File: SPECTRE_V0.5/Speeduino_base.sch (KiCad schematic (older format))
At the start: 185 parts, among them J1 Conn_01x04_Male, J2 Conn_02x04_Odd_Even, J3 Conn_01x06_Male, Q1 2N7002, Q10 BSP78, Q11 BSP78, Q12 BSP78, Q13 BSP78, Q14 BSP78, Q15 BSP78, Q16 BSP78, Q17 BSP78, Q18 BSP78, Q2 CJ2302, Q3 CJ2302, Q4 CJ2302, Q5 BSP78, Q6 BSP78, Q7 CJ2302, Q8 CJ2302, Q9 CJ2302, U1 MAX9926UAEE+, U2 molex_48pin, U3 LM78M05_TO220, U4 MAX3232

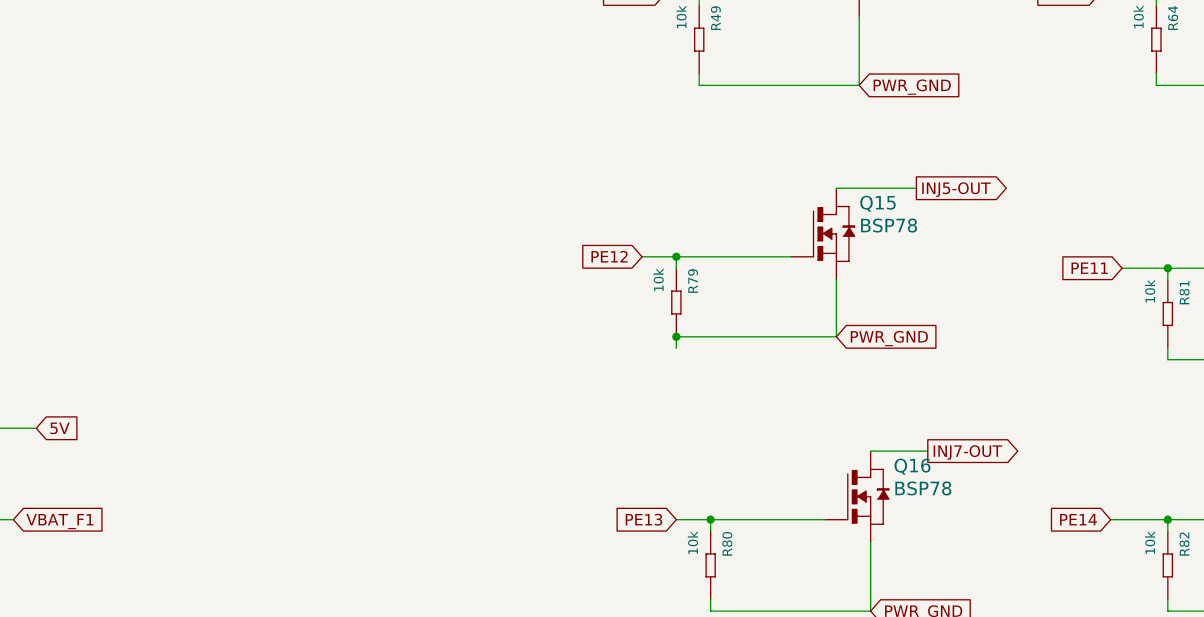
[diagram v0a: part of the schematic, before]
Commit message: update silkscreen
Updated silkscreen V0.4. Start switchable flyback diode in V0.5 for PWM control of injectors
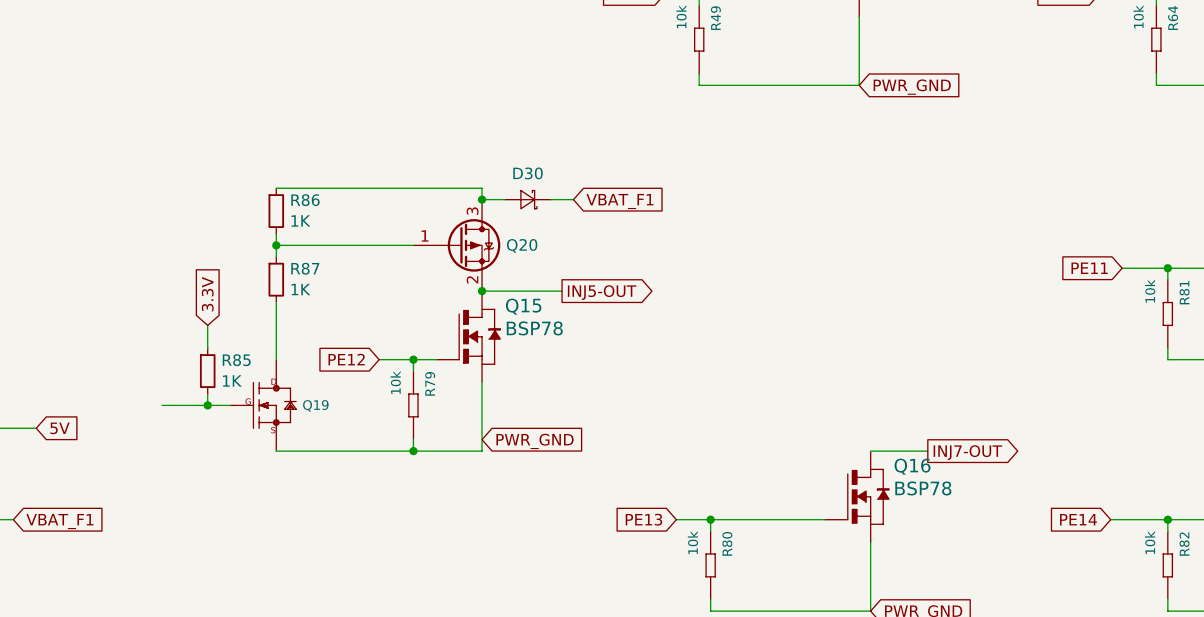
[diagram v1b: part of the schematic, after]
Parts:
- added D30: SS310, Diode_SMD:D_SMA, symbol Device:D_Schottky_Small
- added Q19: SMD-MOSFET-N-CH-30V-5.8A-AO3400(SOT-23), Package_TO_SOT_SMD:SOT-23_Handsoldering, symbol speeduino_lib:SMD-MOSFET-N-CH-30V-5.8A-AO3400(SOT-23)
- added Q20: AO3401A, Package_TO_SOT_SMD:SOT-23, symbol Transistor_FET:AO3401A
- added R85, R86, R87: 1K, Resistor_SMD:R_0603_1608Metric_Pad1.05x0.95mm_HandSolder, symbol Device:R_Small
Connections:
- wire segments 502 -> 515
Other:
- moved on the sheet: Q15, R79
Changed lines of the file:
@@
 	14100 11500 14100 11200
 Wire Wire Line
-	13950 10300 13950 10050
-Wire Wire Line
 	15400 10350 15400 10400
 Wire Wire Line
@@
 	16100 11500 16100 11200
 Wire Wire Line
-	13250 10000 13250 9950
+	12100 10450 12100 10400
 Wire Wire Line
 	15400 10050 15400 10000
@@
 L Speeduino_base-eagle-import:NMOSSOT223 Q15
 U 1 1 6231F413
-P 13950 9850
-F 0 "Q15" H 14050 9950 59  0000 L BNN
-F 1 "BSP78" H 14050 9850 59  0000 L BNN
-F 2 "Speeduino_base:SOT223" H 13950 9850 50  0001 C CNN
-F 3 "" H 13950 9850 50  0001 C CNN
-	1    13950 9850
+P 12400 10300
+F 0 "Q15" H 12500 10400 59  0000 L BNN
+F 1 "BSP78" H 12500 10300 59  0000 L BNN
+F 2 "Speeduino_base:SOT223" H 12400 10300 50  0001 C CNN
+F 3 "" H 12400 10300 50  0001 C CNN
+	1    12400 10300
 	1    0    0    -1
 $EndComp
@@
 L Speeduino_base-eagle-import:SMD-RES-470R-5%-1_10W(0603) R79
 U 1 1 6231F42B
-P 13250 10150
-F 0 "R79" H 13100 10200 42  0000 L BNN
-F 1 "10k" H 13100 10050 42  0000 L BNN
-F 2 "Speeduino_base:R0603" H 13250 10150 50  0001 C CNN
-F 3 "" H 13250 10150 50  0001 C CNN
-	1    13250 10150
+P 12100 10600
+F 0 "R79" H 11950 10650 42  0000 L BNN
+F 1 "10k" H 11950 10500 42  0000 L BNN
+F 2 "Speeduino_base:R0603" H 12100 10600 50  0001 C CNN
+F 3 "" H 12100 10600 50  0001 C CNN
+	1    12100 10600
 	0    1    1    0
 $EndComp
@@
 	0    1    1    0
 $EndComp
-Text GLabel 13100 9950 0    50   Input ~ 0
+Text GLabel 11950 10400 0    50   Input ~ 0
 PE12
 Text GLabel 13250 11100 0    50   Input ~ 0
@@
 PE14
 Wire Wire Line
-	13100 9950 13250 9950
-Connection ~ 13250 9950
-Wire Wire Line
-	13250 9950 13750 9950
+	11950 10400 12100 10400
 Wire Wire Line
 	13250 11100 13400 11100
@@
 Wire Wire Line
 	15400 11100 15900 11100
-Text GLabel 14300 9650 2    50   Output ~ 0
+Text GLabel 12750 10100 2    50   Output ~ 0
 INJ5-OUT
 Text GLabel 14350 10800 2    50   Output ~ 0
@@
 INJ6-OUT
 Wire Wire Line
-	13950 9650 14300 9650
-Wire Wire Line
 	14100 10800 14350 10800
 Wire Wire Line
@@
 	16100 10800 16400 10800
 Wire Wire Line
-	13250 10300 13950 10300
-Connection ~ 13250 10300
-Wire Wire Line
-	13250 10300 13250 10350
+	12100 10750 12100 10800
 Text GLabel 14100 11500 2    50   Input ~ 0
 PWR_GND
-Text GLabel 13950 10300 2    50   Input ~ 0
+Text GLabel 12400 10750 2    50   Input ~ 0
 PWR_GND
 Text GLabel 16100 10400 2    50   Input ~ 0
@@
 Text GLabel 14550 5050 1    50   Input ~ 0
 PD8
+$Comp
+L speeduino_lib:SMD-MOSFET-N-CH-30V-5.8A-AO3400(SOT-23) Q19
+U 1 1 5E997814
+P 11500 10600
+F 0 "Q19" H 11614 10600 42  0000 L CNN
+F 1 "SMD-MOSFET-N-CH-30V-5.8A-AO3400(SOT-23)" H 11614 10561 42  0001 L CNN
+F 2 "Package_TO_SOT_SMD:SOT-23_Handsoldering" H 11500 10600 50  0001 C CNN
+F 3 "" H 11500 10600 50  0001 C CNN
+	1    11500 10600
+	1    0    0    -1
+$EndComp
+$Comp
+L Device:R_Small R86
+U 1 1 5EAAD26C
+P 11500 9750
+F 0 "R86" H 11559 9796 50  0000 L CNN
+F 1 "1K" H 11559 9705 50  0000 L CNN
+F 2 "Resistor_SMD:R_0603_1608Metric_Pad1.05x0.95mm_HandSolder" H 11500 9750 50  0001 C CNN
+F 3 "~" H 11500 9750 50  0001 C CNN
+	1    11500 9750
+	1    0    0    -1
+$EndComp
+$Comp
+L Device:R_Small R87
+U 1 1 5EAADD91
+P 11500 10050
+F 0 "R87" H 11559 10096 50  0000 L CNN
+F 1 "1K" H 11559 10005 50  0000 L CNN
+F 2 "Resistor_SMD:R_0603_1608Metric_Pad1.05x0.95mm_HandSolder" H 11500 10050 50  0001 C CNN
+F 3 "~" H 11500 10050 50  0001 C CNN
+	1    11500 10050
+	1    0    0    -1
+$EndComp
+Wire Wire Line
+	12400 10500 12400 10800
+Wire Wire Line
+	12100 10400 12200 10400
+Connection ~ 12100 10400
+Wire Wire Line
+	12400 10100 12750 10100
+Wire Wire Line
+	12800 9700 12700 9700
+Text GLabel 12800 9700 2    50   Input ~ 0
+VBAT_F1
+$Comp
+L Device:D_Schottky_Small D30
+U 1 1 5E84310E
+P 12600 9700
+F 0 "D30" H 12600 9587 50  0000 C CNN
+F 1 "SS310" V 12645 9768 50  0001 L CNN
+F 2 "Diode_SMD:D_SMA" V 12600 9700 50  0001 C CNN
+F 3 "~" V 12600 9700 50  0001 C CNN
+	1    12600 9700
+	-1   0    0    1
+$EndComp
+$Comp
+L Transistor_FET:AO3401A Q20
+U 1 1 5E83F742
+P 12300 9900
+F 0 "Q20" H 12505 9900 50  0000 L CNN
+F 1 "AO3401A" H 12505 9855 50  0001 L CNN
+F 2 "Package_TO_SOT_SMD:SOT-23" H 12500 9825 50  0001 L CIN
+F 3 "http://www.aosmd.com/pdfs/datasheet/AO3401A.pdf" H 12300 9900 50  0001 L CNN
+	1    12300 9900
+	1    0    0    -1
+$EndComp
+Connection ~ 12400 10100
+Wire Wire Line
+	12400 9700 12500 9700
+Wire Wire Line
+	11500 10800 12100 10800
+Connection ~ 12100 10800
+Wire Wire Line
+	12100 10800 12400 10800
+Wire Wire Line
+	11500 10400 11500 10150
+Wire Wire Line
+	11500 9950 11500 9900
+Wire Wire Line
+	11500 9650 12400 9650
+Wire Wire Line
+	12400 9650 12400 9700
+Connection ~ 12400 9700
+Wire Wire Line
+	11500 9900 12100 9900
+Connection ~ 11500 9900
+Wire Wire Line
+	11500 9900 11500 9850
+$Comp
+L Device:R_Small R85
+U 1 1 5EE73862
+P 11200 10450
+F 0 "R85" H 11259 10496 50  0000 L CNN
+F 1 "1K" H 11259 10405 50  0000 L CNN
+F 2 "Resistor_SMD:R_0603_1608Metric_Pad1.05x0.95mm_HandSolder" H 11200 10450 50  0001 C CNN
+F 3 "~" H 11200 10450 50  0001 C CNN
+	1    11200 10450
+	1    0    0    -1
+$EndComp
+Text GLabel 11200 10250 1    50   Input ~ 0
+3.3V
+Wire Wire Line
+	11200 10250 11200 10350
+Wire Wire Line
+	11200 10550 11200 10600
+Wire Wire Line
+	11200 10600 11300 10600
+Wire Wire Line
+	11200 10600 11000 10600
+Connection ~ 11200 10600
 $EndSCHEMATC

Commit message: Routing V0.5
Started routing board V0.5
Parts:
- removed Q16, Q17: BSP78, Speeduino_base:SOT223, symbol Speeduino_base-eagle-import:NMOSSOT223
- removed R80, R81, R82: 10k, Speeduino_base:R0603, symbol Speeduino_base-eagle-import:SMD-RES-470R-5%-1_10W(0603)
- added D31, D32, D33: SS310, Diode_SMD:D_SMA, symbol Device:D_Schottky_Small
- added Q16, Q21, Q22: SMD-MOSFET-N-CH-30V-5.8A-AO3400(SOT-23), Package_TO_SOT_SMD:SOT-23_Handsoldering, symbol speeduino_lib:SMD-MOSFET-N-CH-30V-5.8A-AO3400(SOT-23)
- added Q17, Q23, Q24: AO3401A, Package_TO_SOT_SMD:SOT-23_Handsoldering, symbol Transistor_FET:AO3401A
- added Q25, Q26: BSP78, Speeduino_base:SOT223, symbol Speeduino_base-eagle-import:NMOSSOT223
- added R80, R81, R82, R89, R90, R91, R92, R93, R94: 1K, Speeduino_base:R_0603_1608Metric_Pad1.05x0.95mm_HandSolder, symbol Device:R_Small
- added R88, R95, R96: 10k, Speeduino_base:R_0603_1608Metric_Pad1.05x0.95mm_HandSolder, symbol Speeduino_base-eagle-import:SMD-RES-470R-5%-1_10W(0603)
- Q20: footprint Package_TO_SOT_SMD:SOT-23 -> Package_TO_SOT_SMD:SOT-23_Handsoldering
- R79: footprint Speeduino_base:R0603 -> Speeduino_base:R_0603_1608Metric_Pad1.05x0.95mm_HandSolder
- R85, R86, R87: footprint Resistor_SMD:R_0603_1608Metric_Pad1.05x0.95mm_HandSolder -> Speeduino_base:R_0603_1608Metric_Pad1.05x0.95mm_HandSolder
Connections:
- wire segments 515 -> 554
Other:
- moved on the sheet: D30, Q13, Q15, Q19, Q20, Q6, R49, R64, R79, R85, R86, R87
